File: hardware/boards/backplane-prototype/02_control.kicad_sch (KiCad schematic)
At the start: 15 parts, among them J10 TC2030-IDC-NL SWD, U1 STM32C092GCU6

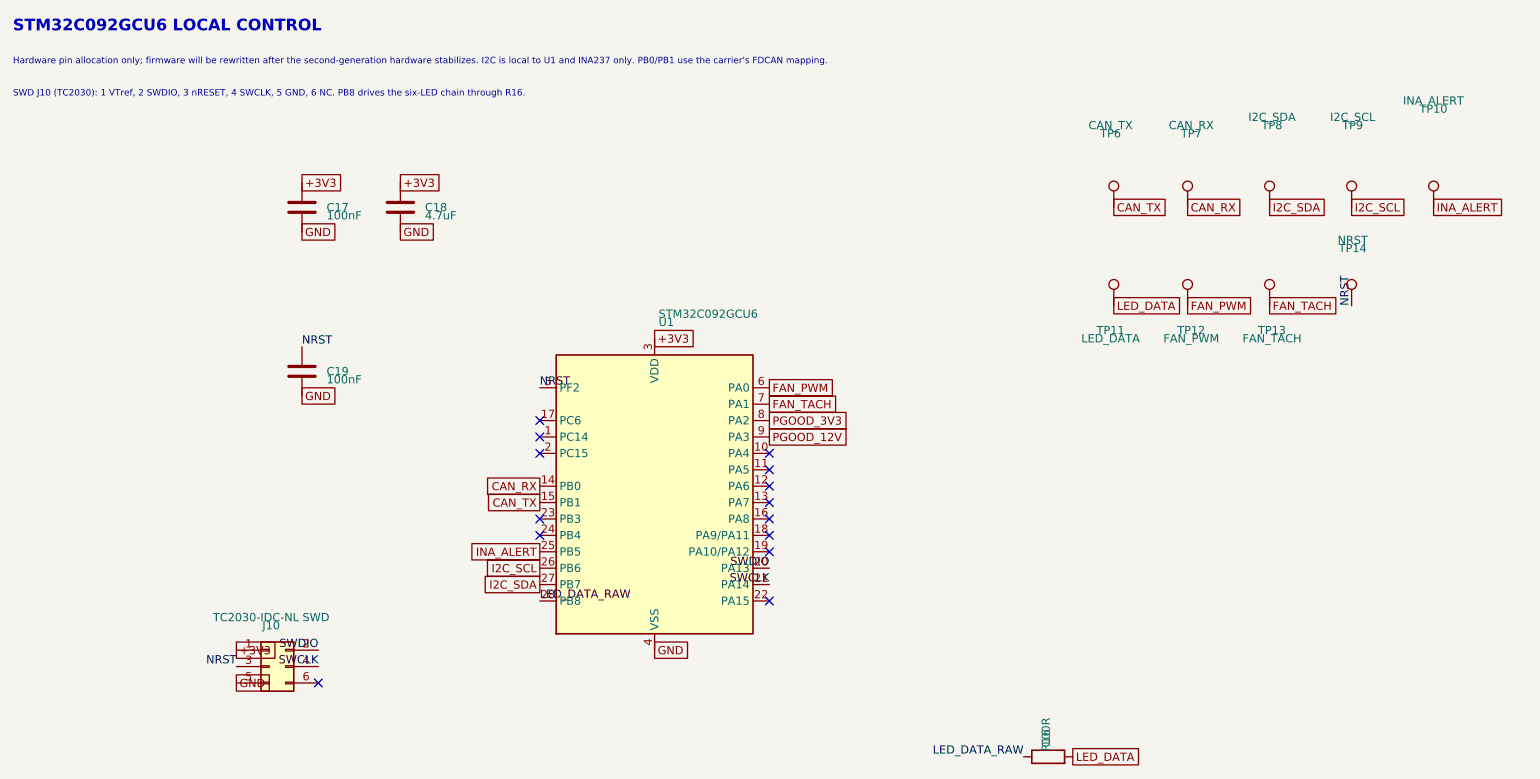
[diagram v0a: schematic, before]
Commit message: checkpoint backplane PCB synchronization
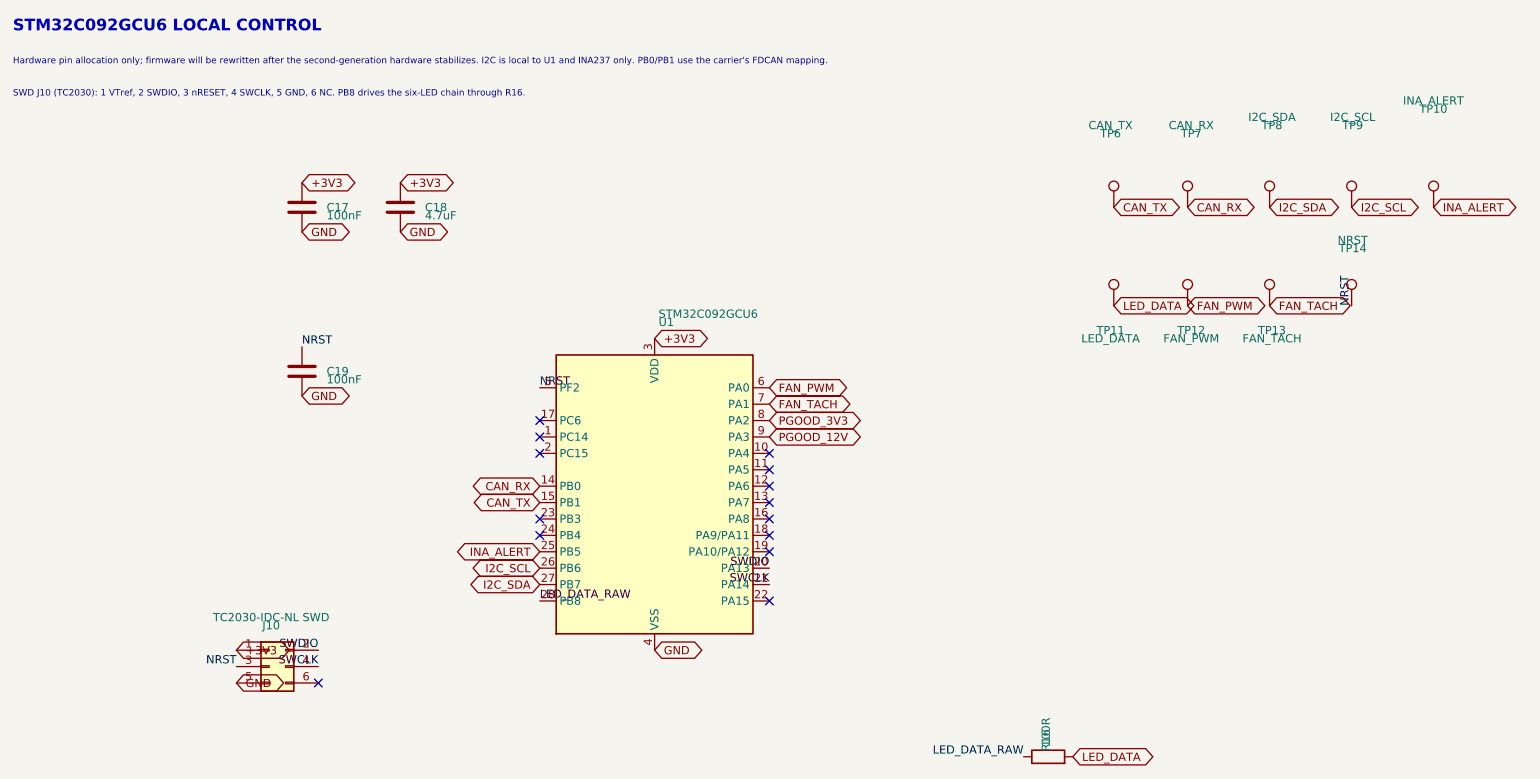
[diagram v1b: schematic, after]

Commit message: hardware: mark all test points DNP
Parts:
- TP10, TP11, TP12, TP13, TP14, TP6, TP7, TP8, TP9: now not fitted; now left out of the parts list
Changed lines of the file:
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@@
 		(body_style 1)
 		(exclude_from_sim no)
-		(in_bom yes)
-		(on_board yes)
-		(in_pos_files yes)
-		(dnp no)
+		(in_bom no)
+		(on_board yes)
+		(in_pos_files yes)
+		(dnp yes)
 		(property "Reference" "TP11"
 			(at 190 63.5 0)
@@
 		(body_style 1)
 		(exclude_from_sim no)
-		(in_bom yes)
-		(on_board yes)
-		(in_pos_files yes)
-		(dnp no)
+		(in_bom no)
+		(on_board yes)
+		(in_pos_files yes)
+		(dnp yes)
 		(property "Reference" "TP13"
 			(at 215 63.5 0)
@@
 		(body_style 1)
 		(exclude_from_sim no)
-		(in_bom yes)
-		(on_board yes)
-		(in_pos_files yes)
-		(dnp no)
+		(in_bom no)
+		(on_board yes)
+		(in_pos_files yes)
+		(dnp yes)
 		(property "Reference" "TP12"
 			(at 202.5 63.5 0)
@@
 		(body_style 1)
 		(exclude_from_sim no)
-		(in_bom yes)
-		(on_board yes)
-		(in_pos_files yes)
-		(dnp no)
+		(in_bom no)
+		(on_board yes)
+		(in_pos_files yes)
+		(dnp yes)
 		(property "Reference" "TP7"
 			(at 202.5 33.02 0)
@@
 		(body_style 1)
 		(exclude_from_sim no)
-		(in_bom yes)
-		(on_board yes)
-		(in_pos_files yes)
-		(dnp no)
+		(in_bom no)
+		(on_board yes)
+		(in_pos_files yes)
+		(dnp yes)
 		(property "Reference" "TP6"
 			(at 190 33.02 0)
@@
 		(body_style 1)
 		(exclude_from_sim no)
-		(in_bom yes)
-		(on_board yes)
-		(in_pos_files yes)
-		(dnp no)
+		(in_bom no)
+		(on_board yes)
+		(in_pos_files yes)
+		(dnp yes)
 		(property "Reference" "TP14"
 			(at 227.5 50.8 0)
@@
 		(body_style 1)
 		(exclude_from_sim no)
-		(in_bom yes)
-		(on_board yes)
-		(in_pos_files yes)
-		(dnp no)
+		(in_bom no)
+		(on_board yes)
+		(in_pos_files yes)
+		(dnp yes)
 		(property "Reference" "TP8"
 			(at 215 31.75 0)
@@
 		(body_style 1)
 		(exclude_from_sim no)
-		(in_bom yes)
-		(on_board yes)
-		(in_pos_files yes)
-		(dnp no)
+		(in_bom no)
+		(on_board yes)
+		(in_pos_files yes)
+		(dnp yes)
 		(property "Reference" "TP10"
 			(at 240 29.21 0)
@@
 		(body_style 1)
 		(exclude_from_sim no)
-		(in_bom yes)
-		(on_board yes)
-		(in_pos_files yes)
-		(dnp no)
+		(in_bom no)
+		(on_board yes)
+		(in_pos_files yes)
+		(dnp yes)
 		(property "Reference" "TP9"
 			(at 227.5 31.75 0)

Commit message: hardware: add backplane thermal interfaces
Add a second independent 3-wire fan channel and externally powered DS18B20 header, remove the slot NeoPixels, document the shared fan-rail limits, keep test points out of assembly exports, and move the four chassis holes to their nearest DRC-legal edge positions.
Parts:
- removed R16: 100R, Resistor_SMD:R_0603_1608Metric, symbol Device:R
- removed TP11: LED_DATA, TestPoint:TestPoint_Pad_D1.5mm, symbol Connector:TestPoint
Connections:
- net FAN2_PWM: now reaches U1.12 (PA6)
- net FAN2_TACH: now reaches U1.13 (PA7)
- net LED_DATA_RAW renamed DS18B20_DATA
- no-connect marks 14 -> 12
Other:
- note added: "SWD J10 (TC2030): 1 VTref, 2 SWDIO, 3 nRESET, 4 SWCLK, 5 GND, 6 NC. PA6/PA7 provide TIM3 fan-2 PWM/tach; PB8 is the DS18B20 1-Wire bus."
- note removed: "SWD J10 (TC2030): 1 VTref, 2 SWDIO, 3 nRESET, 4 SWCLK, 5 GND, 6 NC. PB8 drives the six-LED chain through R16."
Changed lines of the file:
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@@
 	(generator_version "10.0")
 	(paper "A4")
-	(text "SWD J10 (TC2030): 1 VTref, 2 SWDIO, 3 nRESET, 4 SWCLK, 5 GND, 6 NC. PB8 drives the six-LED chain through R16."
+	(text "SWD J10 (TC2030): 1 VTref, 2 SWDIO, 3 nRESET, 4 SWCLK, 5 GND, 6 NC. PA6/PA7 provide TIM3 fan-2 PWM/tach; PB8 is the DS18B20 1-Wire bus."
 		(exclude_from_sim no)
 		(at 20 27.5 0)
@@
 		(at 101.6 80.01)
 	)
-	(no_connect
-		(at 137.16 87.63)
+	(global_label "FAN2_PWM"
+		(shape bidirectional)
+		(at 137.16 87.63 0)
+		(effects
+			(font
+				(size 1.27 1.27)
+			)
+			(justify left)
+		)
+		(property "Intersheetrefs" "${INTERSHEET_REFS}"
+			(at 137.16 87.63 0)
+			(hide yes)
+			(show_name no)
+			(do_not_autoplace no)
+			(effects
+				(font
+					(size 1.27 1.27)
+				)
+			)
+		)
 	)
 	(no_connect
 		(at 137.16 82.55)
 	)
-	(no_connect
-		(at 137.16 90.17)
+	(global_label "FAN2_TACH"
+		(shape bidirectional)
+		(at 137.16 90.17 0)
+		(effects
+			(font
+				(size 1.27 1.27)
+			)
+			(justify left)
+		)
+		(property "Intersheetrefs" "${INTERSHEET_REFS}"
+			(at 137.16 90.17 0)
+			(hide yes)
+			(show_name no)
+			(do_not_autoplace no)
+			(effects
+				(font
+					(size 1.27 1.27)
+				)
+			)
+		)
 	)
 	(no_connect
@@
 		)
 	)
-	(label "LED_DATA_RAW"
-		(at 101.6 105.41 0)
-		(effects
-			(font
-				(size 1.27 1.27)
-			)
-			(justify left bottom)
-		)
-	)
-	(label "LED_DATA_RAW"
-		(at 176.53 129.54 180)
-		(effects
-			(font
-				(size 1.27 1.27)
-			)
-			(justify right bottom)
+	(global_label "DS18B20_DATA"
+		(shape bidirectional)
+		(at 101.6 105.41 180)
+		(effects
+			(font
+				(size 1.27 1.27)
+			)
+			(justify right)
+		)
+		(property "Intersheetrefs" "${INTERSHEET_REFS}"
+			(at 101.6 105.41 0)
+			(hide yes)
+			(show_name no)
+			(do_not_autoplace no)
+			(effects
+				(font
+					(size 1.27 1.27)
+				)
+			)
 		)
 	)
@@
 		)
 	)
-	(global_label "LED_DATA"
-		(shape bidirectional)
-		(at 190.5 59.69 0)
-		(effects
-			(font
-				(size 1.27 1.27)
-			)
-			(justify left)
-		)
-		(property "Intersheetrefs" "${INTERSHEET_REFS}"
-			(at 190.5 59.69 0)
-			(hide yes)
-			(show_name no)
-			(do_not_autoplace no)
-			(effects
-				(font
-					(size 1.27 1.27)
-				)
-			)
-		)
-	)
 	(global_label "PGOOD_12V"
 		(shape bidirectional)
@@
 		(property "Intersheetrefs" "${INTERSHEET_REFS}"
 			(at 201.93 44.45 0)
-			(hide yes)
-			(show_name no)
-			(do_not_autoplace no)
-			(effects
-				(font
-					(size 1.27 1.27)
-				)
-			)
-		)
-	)
-	(global_label "LED_DATA"
-		(shape bidirectional)
-		(at 184.15 129.54 0)
-		(effects
-			(font
-				(size 1.27 1.27)
-			)
-			(justify left)
-		)
-		(property "Intersheetrefs" "${INTERSHEET_REFS}"
-			(at 184.15 129.54 0)
 			(hide yes)
 			(show_name no)
@@
 	(symbol
 		(lib_id "Connector:TestPoint")
-		(at 190.5 59.69 0)
-		(unit 1)
-		(body_style 1)
-		(exclude_from_sim no)
-		(in_bom no)
-		(on_board yes)
-		(in_pos_files yes)
-		(dnp yes)
-		(property "Reference" "TP11"
-			(at 190 63.5 0)
-			(show_name no)
-			(do_not_autoplace no)
-			(effects
-				(font
-					(size 1.27 1.27)
-				)
-			)
-		)
-		(property "Value" "LED_DATA"
-			(at 190 64.77 0)
-			(show_name no)
-			(do_not_autoplace no)
-			(effects
-				(font
-					(size 1.27 1.27)
-				)
-			)
-		)
-		(property "Footprint" "TestPoint:TestPoint_Pad_D1.5mm"
-			(at 195.08 60 0)
-			(hide yes)
-			(show_name no)
-			(do_not_autoplace no)
-			(effects
-				(font
-					(size 1.27 1.27)
-				)
-			)
-		)
-		(property "Datasheet" ""
-			(at 195.08 60 0)
-			(hide yes)
-			(show_name no)
-			(do_not_autoplace no)
-			(effects
-				(font
-					(size 1.27 1.27)
-				)
-			)
-		)
-		(property "Description" "test point"
-			(at 190 60 0)
-			(hide yes)
-			(show_name no)
-			(do_not_autoplace no)
-			(effects
-				(font
-					(size 1.27 1.27)
-				)
-			)
-		)
-		(pin "1"
-		)
-		(instances
-			(project "backplane-prototype"
-				(path "/348cc909-6345-4013-9bef-98714057a65b/4275522b-7aaa-4a22-8d94-d30e15c87e30"
-					(reference "TP11")
-					(unit 1)
-				)
-			)
-		)
-	)
-	(symbol
-		(lib_id "Connector:TestPoint")
 		(at 214.63 59.69 0)
 		(unit 1)
@@
 					(unit 1)
 				)
-			)
-		)
-	)
-	(symbol
-		(lib_id "Device:R")
-		(at 180.34 129.54 90)
-		(unit 1)
-		(body_style 1)
-		(exclude_from_sim no)
-		(in_bom yes)
-		(on_board yes)
-		(in_pos_files yes)
-		(dnp no)
-		(property "Reference" "R16"
-			(at 180 127 0)
-			(show_name no)
-			(do_not_autoplace no)
-			(effects
-				(font
-					(size 1.27 1.27)
-				)
-			)
-		)
-		(property "Value" "100R"
-			(at 180 125.73 0)
-			(show_name no)
-			(do_not_autoplace no)
-			(effects
-				(font
-					(size 1.27 1.27)
-				)
-			)
-		)
-		(property "Footprint" "Resistor_SMD:R_0603_1608Metric"
-			(at 180 131.778 90)
-			(hide yes)
-			(show_name no)
-			(do_not_autoplace no)
-			(effects
-				(font
-					(size 1.27 1.27)
-				)
-			)
-		)
-		(property "Datasheet" ""
-			(at 180 130 0)
-			(hide yes)
-			(show_name no)
-			(do_not_autoplace no)
-			(effects
-				(font
-					(size 1.27 1.27)
-				)
-			)
-		)
-		(property "Description" ""
-			(at 180 130 0)
-			(hide yes)
-			(show_name no)
-			(do_not_autoplace no)
-			(effects
-				(font
-					(size 1.27 1.27)
-				)
-			)
-		)
-		(property "MPN" "0603WAF1000T5E"
-			(at 180 130 0)
-			(hide yes)
-			(show_name no)
-			(do_not_autoplace no)
-			(effects
-				(font
-					(size 1.27 1.27)
-				)
-			)
-		)
-		(property "Manufacturer" "UNI-ROYAL (Uniroyal Elec)"
-			(at 180 130 0)
-			(hide yes)
-			(show_name no)
-			(do_not_autoplace no)
-			(effects
-				(font
-					(size 1.27 1.27)
-				)
-			)
-		)
-		(property "LCSC" "C22775"
-			(at 180 130 0)
-			(hide yes)
-			(show_name no)
-			(do_not_autoplace no)
-			(effects
-				(font
-					(size 1.27 1.27)
-				)
-			)
-		)
-		(property "Tolerance" "1%"
-			(at 180 130 0)
-			(hide yes)
-			(show_name no)
-			(do_not_autoplace no)
-			(effects
-				(font
-					(size 1.27 1.27)
-				)
-			)
-		)
-		(pin "1"
-		)
-		(pin "2"
-		)
-		(instances
-			(project "backplane-prototype"
-				(path "/348cc909-6345-4013-9bef-98714057a65b/4275522b-7aaa-4a22-8d94-d30e15c87e30"
-					(reference "R16")
-					(unit 1)
-				)

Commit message: checkpoint: save backplane layout updates
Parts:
- removed TP13: FAN_TACH, TestPoint:TestPoint_Pad_D1.5mm, symbol Connector:TestPoint
- removed TP14: NRST, TestPoint:TestPoint_Pad_D1.5mm, symbol Connector:TestPoint
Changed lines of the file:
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@@
 		(at 101.6 80.01)
-	)
-	(global_label "FAN2_PWM"
-		(shape bidirectional)
-		(at 137.16 87.63 0)
-		(effects
-			(font
-				(size 1.27 1.27)
-			)
-			(justify left)
-		)
-		(property "Intersheetrefs" "${INTERSHEET_REFS}"
-			(at 137.16 87.63 0)
-			(hide yes)
-			(show_name no)
-			(do_not_autoplace no)
-			(effects
-				(font
-					(size 1.27 1.27)
-				)
-			)
-		)
 	)
 	(no_connect
 		(at 137.16 82.55)
 	)
-	(global_label "FAN2_TACH"
-		(shape bidirectional)
-		(at 137.16 90.17 0)
-		(effects
-			(font
-				(size 1.27 1.27)
-			)
-			(justify left)
-		)
-		(property "Intersheetrefs" "${INTERSHEET_REFS}"
-			(at 137.16 90.17 0)
-			(hide yes)
-			(show_name no)
-			(do_not_autoplace no)
-			(effects
-				(font
-					(size 1.27 1.27)
-				)
-			)
-		)
-	)
 	(no_connect
 		(at 137.16 92.71)
@@
 		)
 	)
-	(global_label "DS18B20_DATA"
-		(shape bidirectional)
-		(at 101.6 105.41 180)
-		(effects
-			(font
-				(size 1.27 1.27)
-			)
-			(justify right)
-		)
-		(property "Intersheetrefs" "${INTERSHEET_REFS}"
-			(at 101.6 105.41 0)
-			(hide yes)
-			(show_name no)
-			(do_not_autoplace no)
-			(effects
-				(font
-					(size 1.27 1.27)
-				)
-			)
-		)
-	)
 	(label "SWCLK"
 		(at 67.31 115.57 180)
@@
 		)
 	)
-	(label "NRST"
-		(at 227.33 59.69 90)
-		(effects
-			(font
-				(size 1.27 1.27)
-			)
-			(justify left bottom)
-		)
-	)
 	(label "SWCLK"
 		(at 137.16 102.87 180)
@@
 		)
 	)
+	(global_label "DS18B20_DATA"
+		(shape bidirectional)
+		(at 101.6 105.41 180)
+		(effects
+			(font
+				(size 1.27 1.27)
+			)
+			(justify right)
+		)
+		(property "Intersheetrefs" "${INTERSHEET_REFS}"
+			(at 101.6 105.41 0)
+			(hide yes)
+			(show_name no)
+			(do_not_autoplace no)
+			(effects
+				(font
+					(size 1.27 1.27)
+				)
+			)
+		)
+	)
 	(global_label "+3V3"
 		(shape bidirectional)
@@
 		)
 	)
+	(global_label "FAN2_TACH"
+		(shape bidirectional)
+		(at 137.16 90.17 0)
+		(effects
+			(font
+				(size 1.27 1.27)
+			)
+			(justify left)
+		)
+		(property "Intersheetrefs" "${INTERSHEET_REFS}"
+			(at 137.16 90.17 0)
+			(hide yes)
+			(show_name no)
+			(do_not_autoplace no)
+			(effects
+				(font
+					(size 1.27 1.27)
+				)
+			)
+		)
+	)
 	(global_label "PGOOD_3V3"
 		(shape bidirectional)
@@
 		)
 	)
+	(global_label "FAN2_PWM"
+		(shape bidirectional)
+		(at 137.16 87.63 0)
+		(effects
+			(font
+				(size 1.27 1.27)
+			)
+			(justify left)
+		)
+		(property "Intersheetrefs" "${INTERSHEET_REFS}"
+			(at 137.16 87.63 0)
+			(hide yes)
+			(show_name no)
+			(do_not_autoplace no)
+			(effects
+				(font
+					(size 1.27 1.27)
+				)
+			)
+		)
+	)
 	(global_label "I2C_SDA"
 		(shape bidirectional)
@@
 		(property "Intersheetrefs" "${INTERSHEET_REFS}"
 			(at 64.77 48.26 0)
-			(hide yes)
-			(show_name no)
-			(do_not_autoplace no)
-			(effects
-				(font
-					(size 1.27 1.27)
-				)
-			)
-		)
-	)
-	(global_label "FAN_TACH"
-		(shape bidirectional)
-		(at 214.63 59.69 0)
-		(effects
-			(font
-				(size 1.27 1.27)
-			)
-			(justify left)
-		)
-		(property "Intersheetrefs" "${INTERSHEET_REFS}"
-			(at 214.63 59.69 0)
 			(hide yes)
 			(show_name no)
@@
 	(symbol
 		(lib_id "Connector:TestPoint")
-		(at 214.63 59.69 0)
-		(unit 1)
-		(body_style 1)
-		(exclude_from_sim no)
-		(in_bom no)
-		(on_board yes)
-		(in_pos_files yes)
-		(dnp yes)
-		(property "Reference" "TP13"
-			(at 215 63.5 0)
-			(show_name no)
-			(do_not_autoplace no)
-			(effects
-				(font
-					(size 1.27 1.27)
-				)
-			)
-		)
-		(property "Value" "FAN_TACH"
-			(at 215 64.77 0)
-			(show_name no)
-			(do_not_autoplace no)
-			(effects
-				(font
-					(size 1.27 1.27)
-				)
-			)
-		)
-		(property "Footprint" "TestPoint:TestPoint_Pad_D1.5mm"
-			(at 220.08 60 0)
-			(hide yes)
-			(show_name no)
-			(do_not_autoplace no)
-			(effects
-				(font
-					(size 1.27 1.27)
-				)
-			)
-		)
-		(property "Datasheet" ""
-			(at 220.08 60 0)
-			(hide yes)
-			(show_name no)
-			(do_not_autoplace no)
-			(effects
-				(font
-					(size 1.27 1.27)
-				)
-			)
-		)
-		(property "Description" "test point"
-			(at 215 60 0)
-			(hide yes)
-			(show_name no)
-			(do_not_autoplace no)
-			(effects
-				(font
-					(size 1.27 1.27)
-				)
-			)
-		)
-		(pin "1"
-		)
-		(instances
-			(project "backplane-prototype"
-				(path "/348cc909-6345-4013-9bef-98714057a65b/4275522b-7aaa-4a22-8d94-d30e15c87e30"
-					(reference "TP13")
-					(unit 1)
-				)
-			)
-		)
-	)
-	(symbol
-		(lib_id "Connector:TestPoint")
 		(at 201.93 59.69 0)
 		(unit 1)
@@
 					(unit 1)
 				)
-			)
-		)
-	)
-	(symbol
-		(lib_id "Connector:TestPoint")
-		(at 227.33 59.69 0)
-		(unit 1)
-		(body_style 1)
-		(exclude_from_sim no)
-		(in_bom no)
-		(on_board yes)
-		(in_pos_files yes)
-		(dnp yes)
-		(property "Reference" "TP14"
-			(at 227.5 50.8 0)
-			(show_name no)
-			(do_not_autoplace no)
-			(effects
-				(font
-					(size 1.27 1.27)
-				)
-			)
-		)
-		(property "Value" "NRST"
-			(at 227.5 49.53 0)
-			(show_name no)
-			(do_not_autoplace no)
-			(effects
-				(font
-					(size 1.27 1.27)
-				)
-			)
-		)
-		(property "Footprint" "TestPoint:TestPoint_Pad_D1.5mm"
-			(at 232.58 60 0)
-			(hide yes)
-			(show_name no)
-			(do_not_autoplace no)
-			(effects
-				(font
-					(size 1.27 1.27)
-				)
-			)
-		)
-		(property "Datasheet" ""
-			(at 232.58 60 0)
-			(hide yes)
-			(show_name no)
-			(do_not_autoplace no)
-			(effects
-				(font
-					(size 1.27 1.27)
-				)
-			)
-		)
-		(property "Description" "test point"
-			(at 227.5 60 0)
-			(hide yes)
-			(show_name no)
-			(do_not_autoplace no)
-			(effects
-				(font
-					(size 1.27 1.27)
-				)
-			)
-		)
-		(pin "1"
-		)
-		(instances
-			(project "backplane-prototype"
-				(path "/348cc909-6345-4013-9bef-98714057a65b/4275522b-7aaa-4a22-8d94-d30e15c87e30"
-					(reference "TP14")
-					(unit 1)
-				)

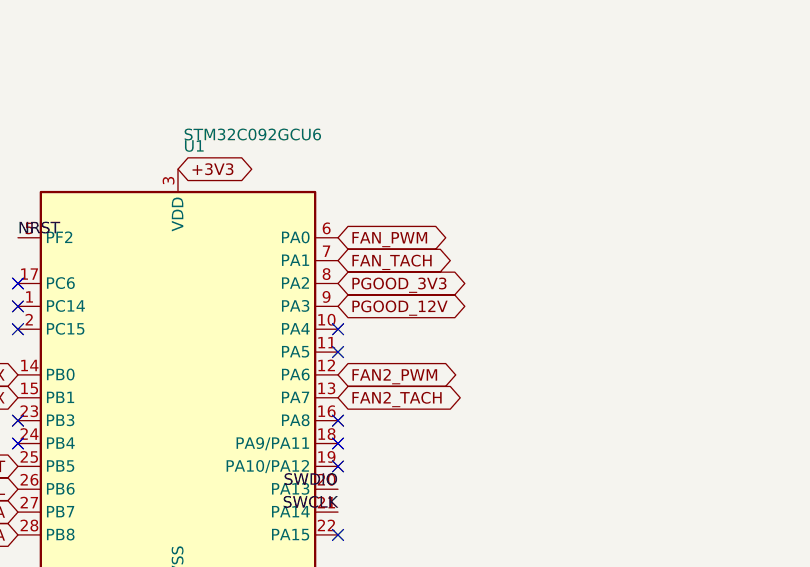
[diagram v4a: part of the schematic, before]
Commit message: hardware: consolidate backplane power and ground zones
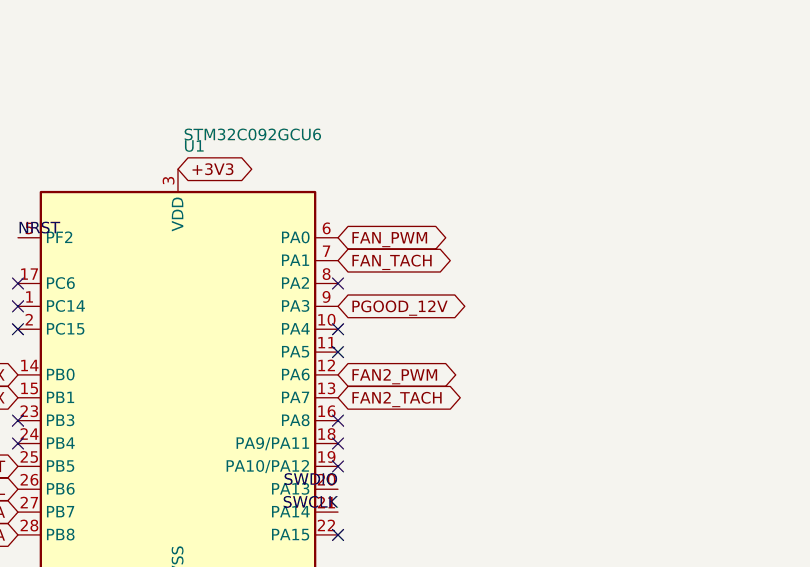
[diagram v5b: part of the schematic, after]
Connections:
- net PGOOD_3V3: no longer names the net of U1.8 (PA2)
- no-connect marks 12 -> 13
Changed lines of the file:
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@@
 		)
 	)
-	(global_label "PGOOD_3V3"
-		(shape bidirectional)
-		(at 137.16 77.47 0)
-		(effects
-			(font
-				(size 1.27 1.27)
-			)
-			(justify left)
-		)
-		(property "Intersheetrefs" "${INTERSHEET_REFS}"
-			(at 137.16 77.47 0)
-			(hide yes)
-			(show_name no)
-			(do_not_autoplace no)
-			(effects
-				(font
-					(size 1.27 1.27)
-				)
-			)
-		)
+	(no_connect
+		(at 137.16 77.47)
 	)
 	(global_label "FAN_TACH"
